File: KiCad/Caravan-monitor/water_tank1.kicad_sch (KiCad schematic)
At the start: 3 parts, among them J4 Coolant temp

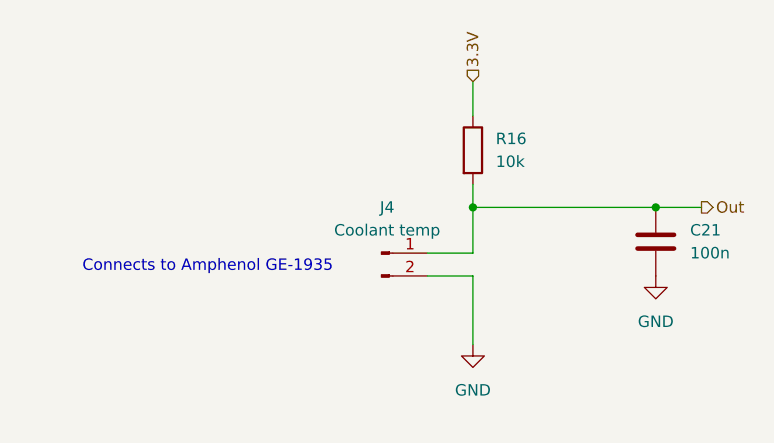
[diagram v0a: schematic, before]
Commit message: Display schematics
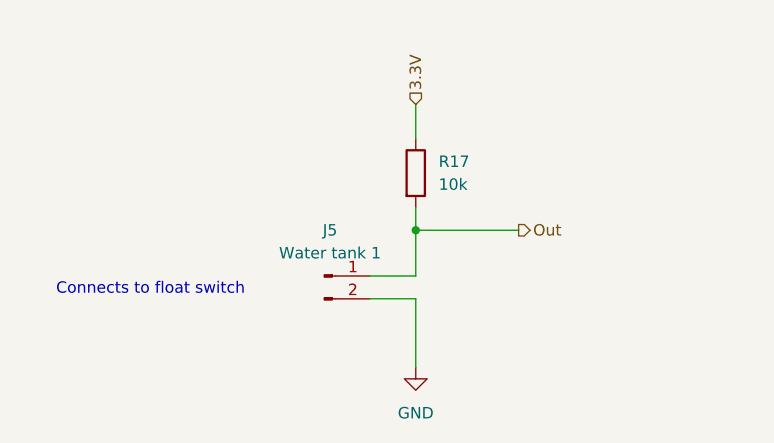
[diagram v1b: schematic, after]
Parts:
- removed C21: 100n, Capacitor_SMD:C_0805_2012Metric_Pad1.18x1.45mm_HandSolder, symbol Device:C
- removed J4: Coolant temp, Connector_JST:JST_XH_S2B-XH-A-1_1x02_P2.50mm_Horizontal, symbol Connector:Conn_01x02_Pin
- removed R16: 10k, Resistor_SMD:R_0805_2012Metric_Pad1.20x1.40mm_HandSolder, symbol Device:R
- added J5: Water tank 1, Connector_JST:JST_XH_S2B-XH-A-1_1x02_P2.50mm_Horizontal, symbol Connector:Conn_01x02_Pin
- added R17: 10k, Resistor_SMD:R_0805_2012Metric_Pad1.20x1.40mm_HandSolder, symbol Device:R
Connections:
- net 3.3V: now also R17.1
- net GND: now also J5.2 (Pin_2)
- net Out: now also J5.1 (Pin_1), R17.2
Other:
- note added: "Connects to float switch"
- note removed: "Connects to Amphenol GE-1935"

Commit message: Schematics done
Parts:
- R17: footprint Resistor_SMD:R_0805_2012Metric_Pad1.20x1.40mm_HandSolder -> Resistor_SMD:R_0402_1005Metric_Pad0.72x0.64mm_HandSolder
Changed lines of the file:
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@@
 			)
 		)
-		(property "Footprint" "Resistor_SMD:R_0805_2012Metric_Pad1.20x1.40mm_HandSolder"
+		(property "Footprint" "Resistor_SMD:R_0402_1005Metric_Pad0.72x0.64mm_HandSolder"
 			(at 134.112 87.63 90)
 			(effects

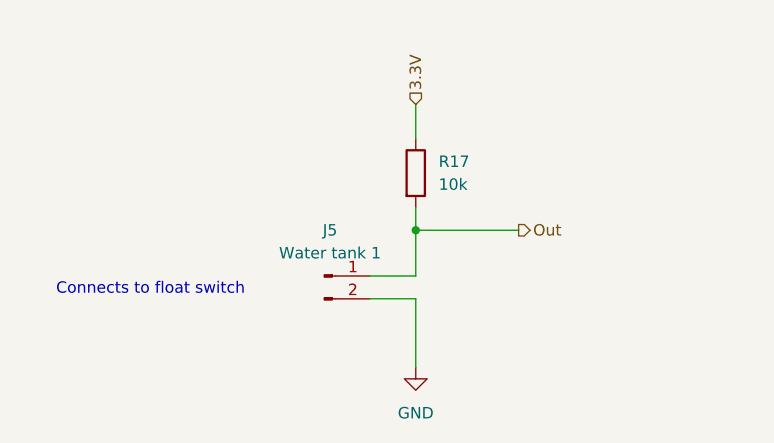
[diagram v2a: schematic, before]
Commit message: Schematic updates
Parts changed for JLCPCB assembly compatibility
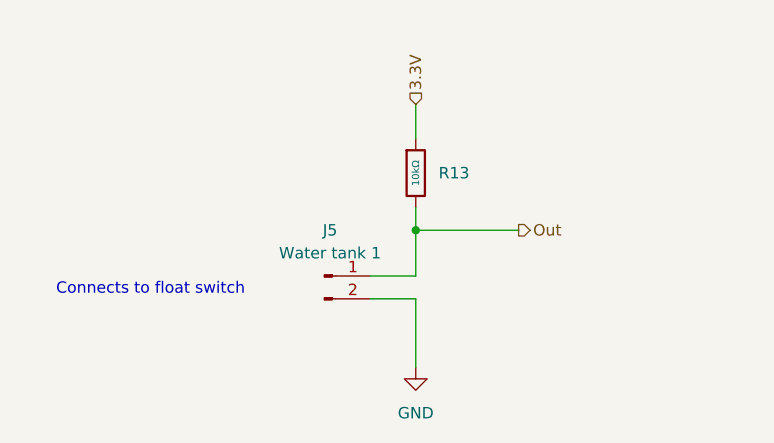
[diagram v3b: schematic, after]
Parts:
- removed R17: 10k, Resistor_SMD:R_0402_1005Metric_Pad0.72x0.64mm_HandSolder, symbol Device:R
- added R13: 10kΩ, PCM_JLCPCB:R_0402, symbol PCM_JLCPCB-Resistors:0402,10kΩ
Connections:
- net 3.3V: now also R13.1
- net Out: now also R13.2
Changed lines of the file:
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@@
 	)
 	(symbol
-		(lib_id "Device:R")
+		(lib_id "PCM_JLCPCB-Resistors:0402,10kΩ")
 		(at 135.89 87.63 0)
 		(unit 1)
@@
 		(dnp no)
 		(fields_autoplaced yes)
-		(property "Reference" "R17"
-			(at 138.43 86.3599 0)
+		(property "Reference" "R13"
+			(at 138.43 87.6299 0)
 			(effects
 				(font
@@
 			)
 		)
-		(property "Value" "10k"
-			(at 138.43 88.8999 0)
-			(effects
-				(font
-					(size 1.27 1.27)
-				)
-				(justify left)
-			)
-		)
-		(property "Footprint" "Resistor_SMD:R_0402_1005Metric_Pad0.72x0.64mm_HandSolder"
+		(property "Value" "10kΩ"
+			(at 135.89 87.63 90)
+			(do_not_autoplace yes)
+			(effects
+				(font
+					(size 0.8 0.8)
+				)
+			)
+		)
+		(property "Footprint" "PCM_JLCPCB:R_0402"
 			(at 134.112 87.63 90)
 			(effects
@@
 			)
 		)
-		(property "Datasheet" "~"
-			(at 135.89 87.63 0)
-			(effects
-				(font
-					(size 1.27 1.27)
-				)
-				(hide yes)
-			)
-		)
-		(property "Description" "Resistor"
-			(at 135.89 87.63 0)
-			(effects
-				(font
-					(size 1.27 1.27)
-				)
-				(hide yes)
-			)
+		(property "Datasheet" "https://www.lcsc.com/datasheet/lcsc_datasheet_2411221126_UNI-ROYAL-Uniroyal-Elec-0402WGF1002TCE_C25744.pdf"
+			(at 135.89 87.63 0)
+			(effects
+				(font
+					(size 1.27 1.27)
+				)
+				(hide yes)
+			)
+		)
+		(property "Description" "62.5mW Thick Film Resistors 50V ±100ppm/°C ±1% 10kΩ 0402 Chip Resistor - Surface Mount ROHS"
+			(at 135.89 87.63 0)
+			(effects
+				(font
+					(size 1.27 1.27)
+				)
+				(hide yes)
+			)
+		)
+		(property "LCSC" "C25744"
+			(at 135.89 87.63 0)
+			(effects
+				(font
+					(size 1.27 1.27)
+				)
+				(hide yes)
+			)
+		)
+		(property "Stock" "24372091"
+			(at 135.89 87.63 0)
+			(effects
+				(font
+					(size 1.27 1.27)
+				)
+				(hide yes)
+			)
+		)
+		(property "Price" "0.004USD"
+			(at 135.89 87.63 0)
+			(effects
+				(font
+					(size 1.27 1.27)
+				)
+				(hide yes)
+			)
+		)
+		(property "Process" "SMT"
+			(at 135.89 87.63 0)
+			(effects
+				(font
+					(size 1.27 1.27)
+				)
+				(hide yes)
+			)
+		)
+		(property "Minimum Qty" "20"
+			(at 135.89 87.63 0)
+			(effects
+				(font
+					(size 1.27 1.27)
+				)
+				(hide yes)
+			)
+		)
+		(property "Attrition Qty" "10"
+			(at 135.89 87.63 0)
+			(effects
+				(font
+					(size 1.27 1.27)
+				)
+				(hide yes)
+			)
+		)
+		(property "Class" "Basic Component"
+			(at 135.89 87.63 0)
+			(effects
+				(font
+					(size 1.27 1.27)
+				)
+				(hide yes)
+			)
+		)
+		(property "Category" "Resistors,Chip Resistor - Surface Mount"
+			(at 135.89 87.63 0)
+			(effects
+				(font
+					(size 1.27 1.27)
+				)
+				(hide yes)
+			)
+		)
+		(property "Manufacturer" "UNI-ROYAL(Uniroyal Elec)"
+			(at 135.89 87.63 0)
+			(effects
+				(font
+					(size 1.27 1.27)
+				)
+				(hide yes)
+			)
+		)
+		(property "Part" "0402WGF1002TCE"
+			(at 135.89 87.63 0)
+			(effects
+				(font
+					(size 1.27 1.27)
+				)
+				(hide yes)
+			)
+		)
+		(property "Resistance" "10kΩ"
+			(at 135.89 87.63 0)
+			(effects
+				(font
+					(size 1.27 1.27)
+				)
+				(hide yes)
+			)
+		)
+		(property "Power(Watts)" "62.5mW"
+			(at 135.89 87.63 0)
+			(effects
+				(font
+					(size 1.27 1.27)
+				)
+				(hide yes)
+			)
+		)
+		(property "Type" "Thick Film Resistors"
+			(at 135.89 87.63 0)
+			(effects
+				(font
+					(size 1.27 1.27)
+				)
+				(hide yes)
+			)
+		)
+		(property "Overload Voltage (Max)" "50V"
+			(at 135.89 87.63 0)
+			(effects
+				(font
+					(size 1.27 1.27)
+				)
+				(hide yes)
+			)
+		)
+		(property "Operating Temperature Range" "-55°C~+155°C"
+			(at 135.89 87.63 0)
+			(effects
+				(font
+					(size 1.27 1.27)
+				)
+				(hide yes)
+			)
+		)
+		(property "Tolerance" "±1%"
+			(at 135.89 87.63 0)
+			(effects
+				(font
+					(size 1.27 1.27)
+				)
+				(hide yes)
+			)
+		)
+		(property "Temperature Coefficient" "±100ppm/°C"
+			(at 135.89 87.63 0)
+			(effects
+				(font
+					(size 1.27 1.27)
+				)
+				(hide yes)
+			)
+		)
+		(pin "1"
 		)
 		(pin "2"
 		)
-		(pin "1"
-		)
 		(instances
-			(project "Caravan-monitor"
+			(project ""
 				(path "/4b94aa5f-1c73-4d2e-8117-e53a25103462/a3633ad7-205f-4b33-84d7-ee84b195f250"
-					(reference "R17")
+					(reference "R13")
 					(unit 1)
 				)
